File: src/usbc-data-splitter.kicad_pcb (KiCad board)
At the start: 2 copper layers, 43.7 x 33.2 mm, 3 parts, among them J1 Data, J2 Power, P1 Combined

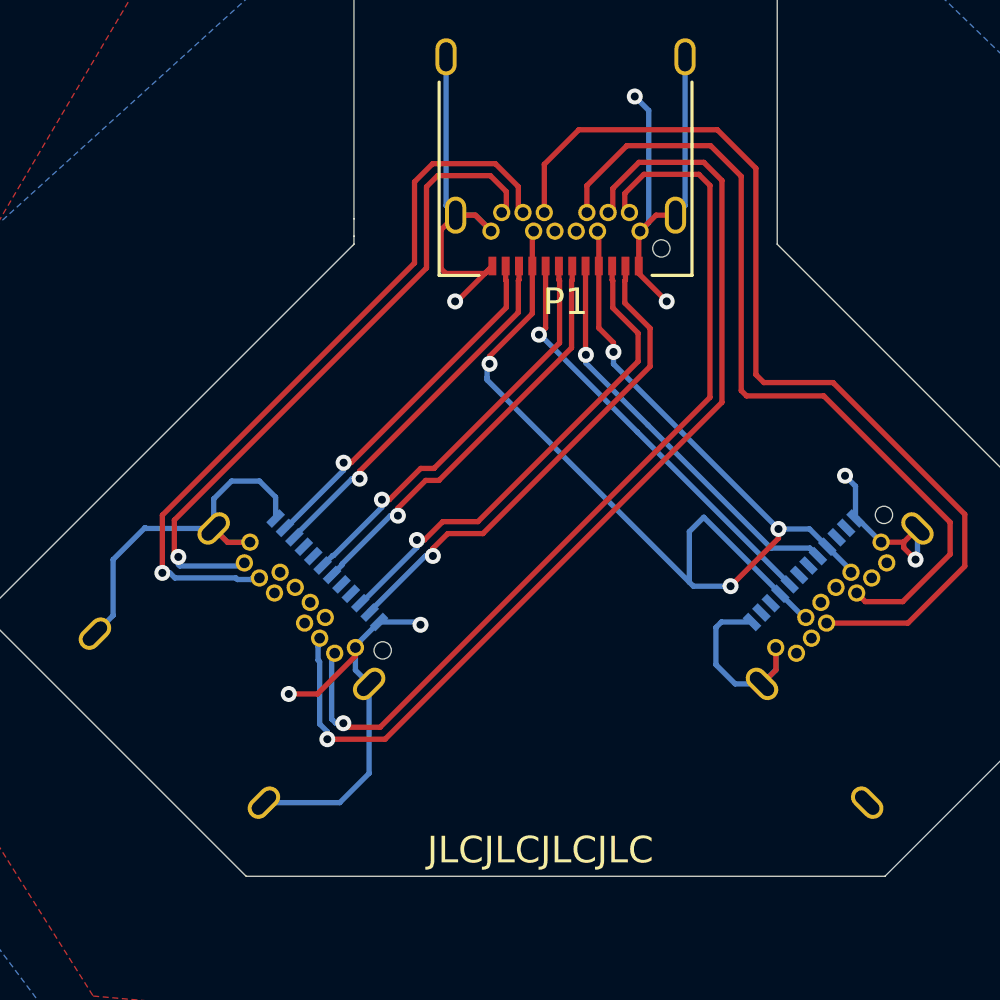
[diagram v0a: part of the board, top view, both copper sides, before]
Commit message: differential pair tuning
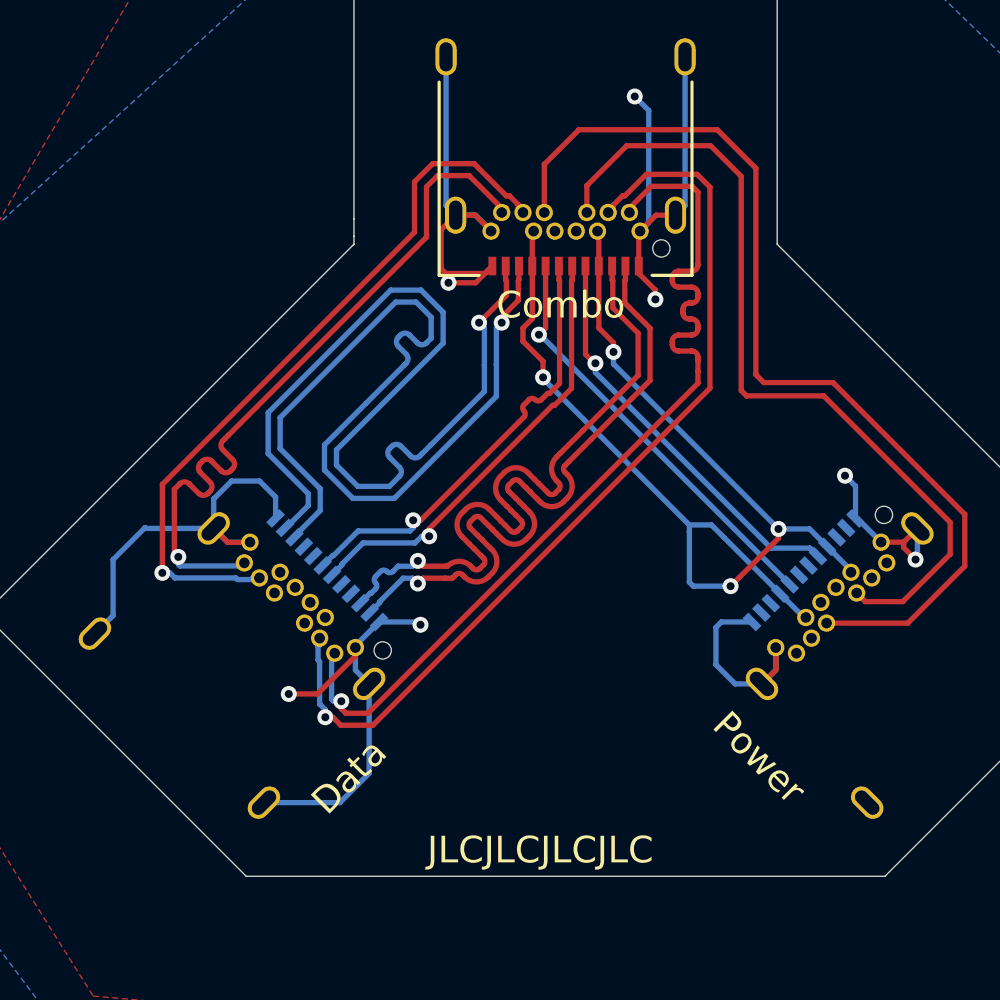
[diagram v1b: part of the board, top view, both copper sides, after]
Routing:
- net RX2_P: track 13.5 -> 35.7 mm
- net RX2_N: track 13.9 -> 35.7 mm
- net TX1_N: track 18.4 -> 26.3 mm
- net TX1_P: track 18.7 -> 26.4 mm
- net VBUS: track 47.1 -> 43.7 mm
- net RX1_N: track 38.1 -> 35.2 mm
- net TX2_P: track 25.0 -> 27.7 mm
- net D_N: track 15.4 -> 16.7 mm
- net D_P: track 15.8 -> 16.7 mm
- net RX1_P: track 34.4 -> 35.1 mm
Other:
- board text added: "Combo"
- board text added: "Data"
- board text added: "Power"
